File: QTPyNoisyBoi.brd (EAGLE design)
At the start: 30.5 x 128.5 mm, 41 parts, among them IC1 LD117AS50TR, IC2 TL074D, J1 WQP-PJ301M-12_JACK, J2 WQP-PJ301M-12_JACK, J3 WQP-PJ301M-12_JACK, J4 WQP-PJ301M-12_JACK, U1 ADAFRUIT_QTPYM0

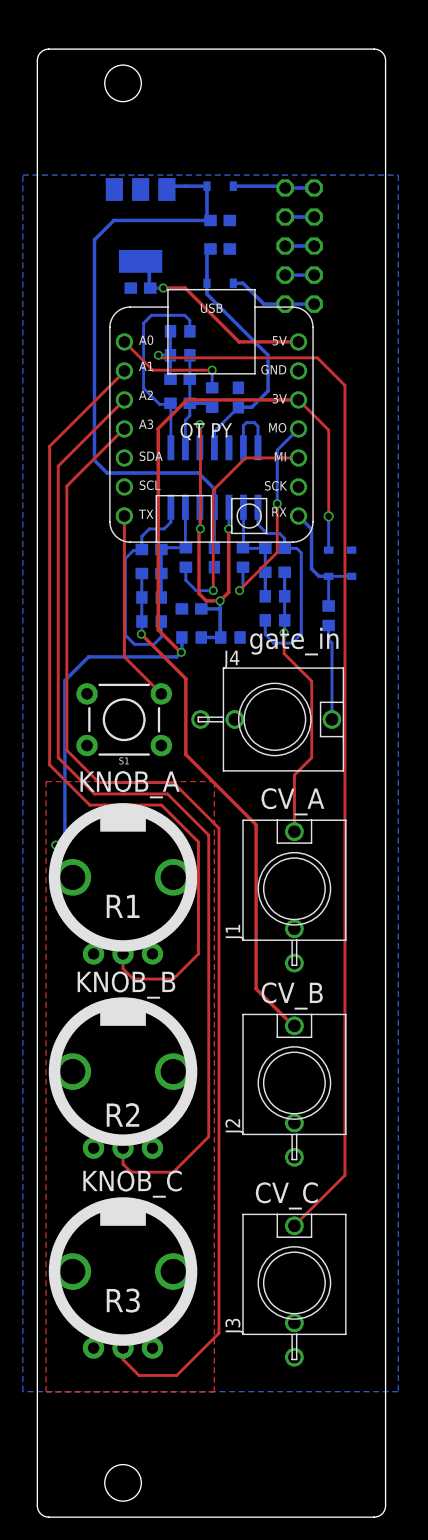
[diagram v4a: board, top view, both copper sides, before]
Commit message: added 2nd button
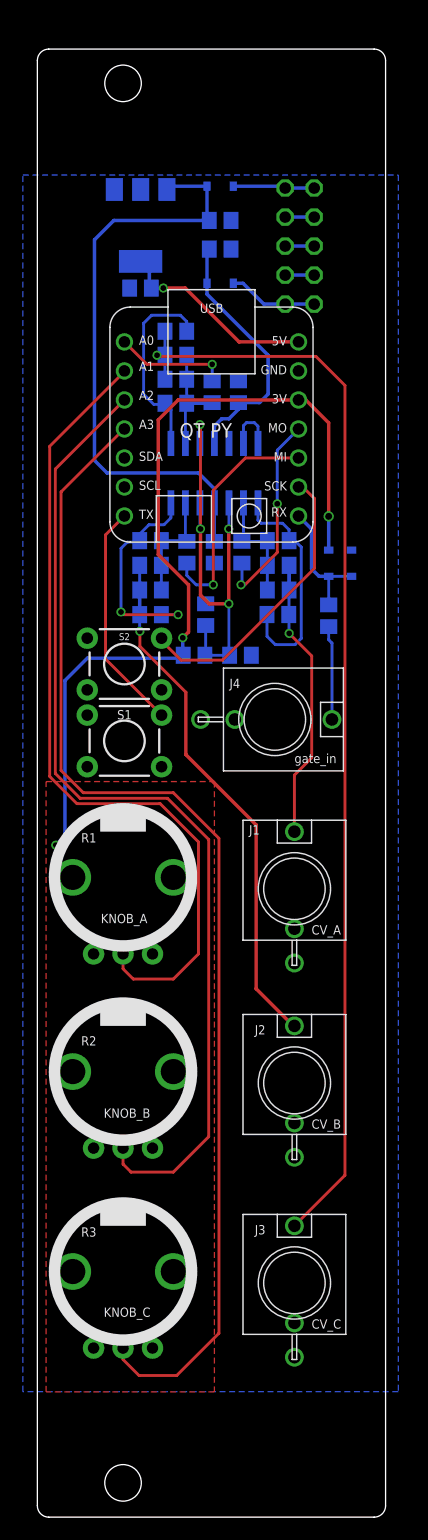
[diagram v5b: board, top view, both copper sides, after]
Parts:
- added S2: PTH-6.0MM, SparkFun-Switches:TACTILE_SWITCH_PTH_6.0MM
- C1, C10, C11, C12, C2, C3, C4, C5, C6, C7, C8, C9: device rcl:C0603 -> rcl:C0805
- R10, R11, R12, R13, R14, R144, R4, R5, R6, R7, R8, R9: device rcl:R0603 -> rcl:R0805
- S1: value MOMENTARY-SWITCH-SPST-PTH-6.0MM -> PTH-6.0MM
- moved S1 1.86 mm to (7.62, 67.9)
- moved R11 1.79 mm to (17.8, 75.4)
- moved R10 1.58 mm to (13.7, 75.4)
- moved C9 1.33 mm to (14.7, 79.0), turned to 270 degrees
- moved C11 0.78 mm to (9.91, 85.5)
- moved C10 0.73 mm to (21.1, 85.5)
- moved C5 0.72 mm to (9.91, 83.3)
- moved C4 0.67 mm to (21.1, 83.3)
- moved R8 0.66 mm to (9.91, 81.2)
- moved R5 0.62 mm to (21.1, 81.2)
- moved R9 0.60 mm to (9.91, 79.0)
- moved R6 0.57 mm to (21.1, 79.0)
- moved C7 0.51 mm to (17.6, 98.5)
- moved R12 0.51 mm to (15.3, 98.5)
- moved R4 0.46 mm to (17.9, 84.5)
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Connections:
- new net SCK: S2.3, U1.SCK
- net GND: now also S2.1
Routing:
- net SCK: track 0.00 -> 25.6 mm
- net VBIAS: track 36.0 -> 39.9 mm
- net N$2: track 16.9 -> 20.1 mm
- net N$10: track 11.8 -> 10.0 mm
- net N$18: track 19.0 -> 20.3 mm
- net A3: track 102.1 -> 103.3 mm
- net A2: track 86.6 -> 87.5 mm
- net N$8: track 5.34 -> 4.57 mm
- net +12V: track 53.6 -> 52.9 mm
- net N$7: track 21.3 -> 20.7 mm
- net N$3: track 18.1 -> 17.4 mm
- net N$6: track 18.5 -> 17.9 mm
- net A1: track 72.0 -> 72.6 mm
- net N$9: track 26.4 -> 27.0 mm
- net N$14: track 19.1 -> 19.2 mm, vias 0 -> 2
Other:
- board text added: "20210407"
- board text removed: "20210331"

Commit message: added neopixels, woorah
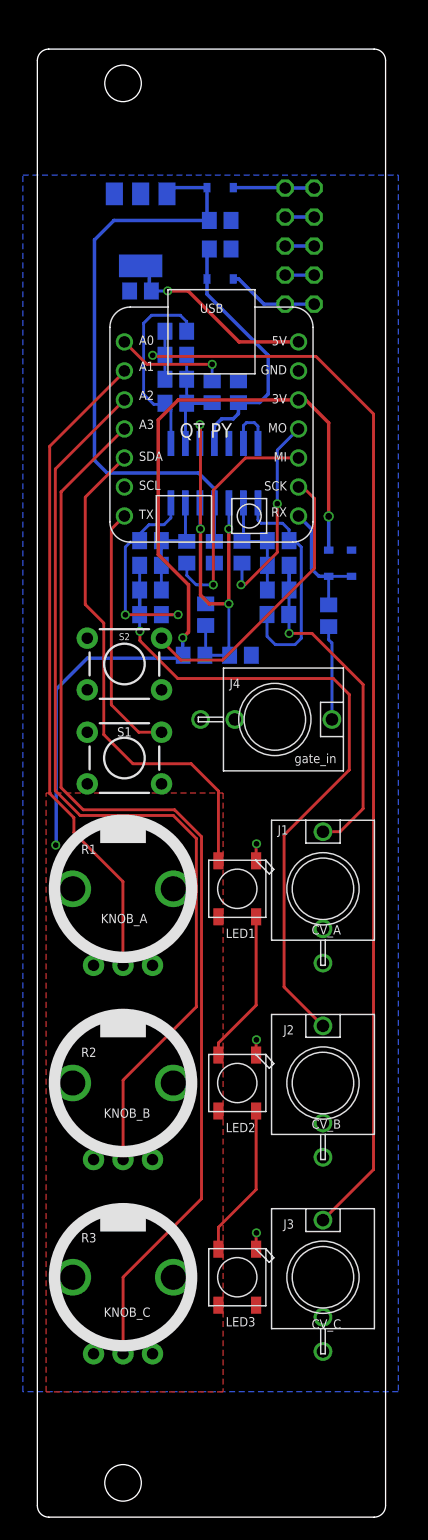
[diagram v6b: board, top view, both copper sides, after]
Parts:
- added LED1, LED2, LED3: WS2812B5050, todstuff:WS2812B
- C4, C5, C8: value 0.1uF -> 10nF
- R15: value 220 -> 200
- moved J3 2.55 mm to (25.0, 21.0)
- moved J1 2.50 mm to (25.0, 55.0)
- moved J2 2.50 mm to (25.0, 38.0)
- moved S1 1.50 mm to (7.62, 66.4)
- moved R1 1.00 mm to (7.50, 55.0)
- moved R2 1.00 mm to (7.50, 38.0)
- moved R3 0.50 mm to (7.50, 21.0)
- moved D4 0.38 mm to (16.0, 108.4)
- moved IC1 0.38 mm to (9.04, 112.7)
- moved C3 0.25 mm to (9.03, 107.3)
- moved D3 0.13 mm to (16.0, 116.4)
- renumbered R144 to R15
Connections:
- new net N$15: LED1.2-DOUT, LED2.4-DIN
- new net N$16: LED2.2-DOUT, LED3.4-DIN
- new net SDA: LED1.4-DIN, U1.SDA
- net +3V3: now also LED1.1-VDD, LED2.1-VDD, LED3.1-VDD
- net GND: now also LED1.3-GND, LED2.3-GND, LED3.3-GND
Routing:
- net SDA: track 0.00 -> 44.5 mm
- net A1: track 72.6 -> 57.4 mm
- net N$1: track 46.0 -> 59.7 mm
- net N$16: track 0.00 -> 13.5 mm
- net N$15: track 0.00 -> 13.5 mm
- net A3: track 103.3 -> 95.9 mm
- net A2: track 87.5 -> 81.5 mm
- net N$9: track 27.0 -> 31.7 mm
- net GND: track 7.62 -> 11.9 mm, vias 0 -> 3
- net N$2: track 20.1 -> 22.4 mm
- net N$11: track 97.8 -> 99.1 mm
- net N$14: track 19.2 -> 18.7 mm
